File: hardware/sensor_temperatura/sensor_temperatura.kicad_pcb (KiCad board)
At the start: 2 copper layers, 18 x 59.1 mm, 7 parts, among them J1 Conn_01x04_Pin, J2 Conn_01x05_Pin, U1 ATtiny85-20P, U3 LM1117T-3.3

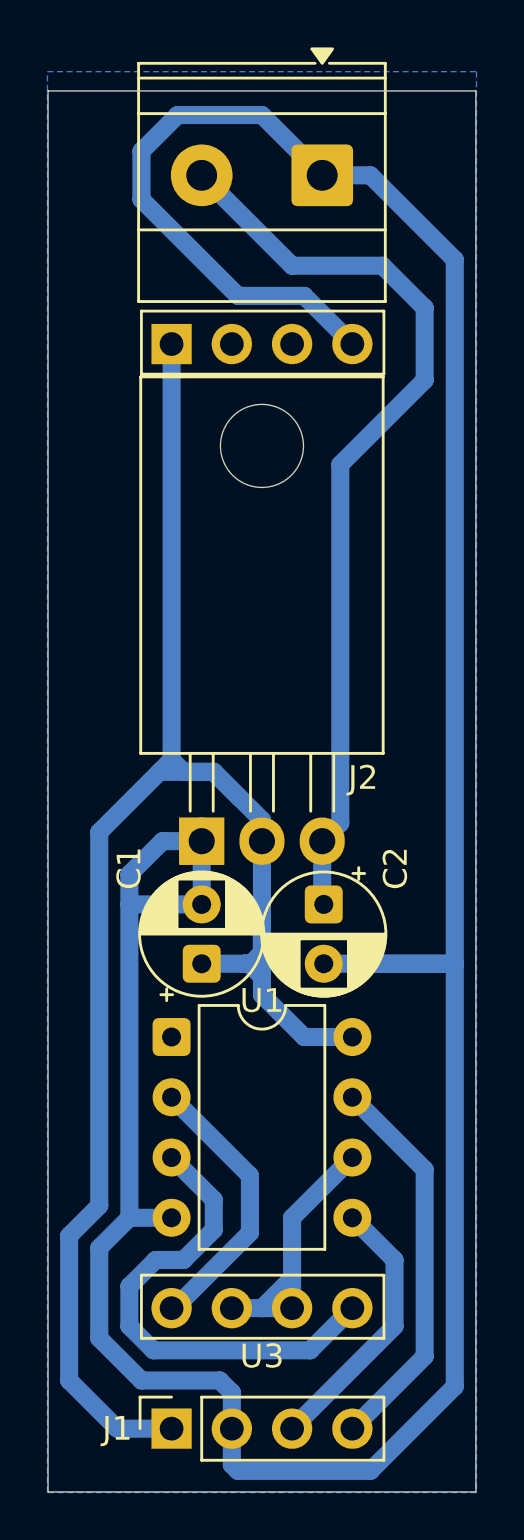
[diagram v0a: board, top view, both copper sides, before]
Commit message: Se actualiza modelo 3d para usar socalo para el micro.
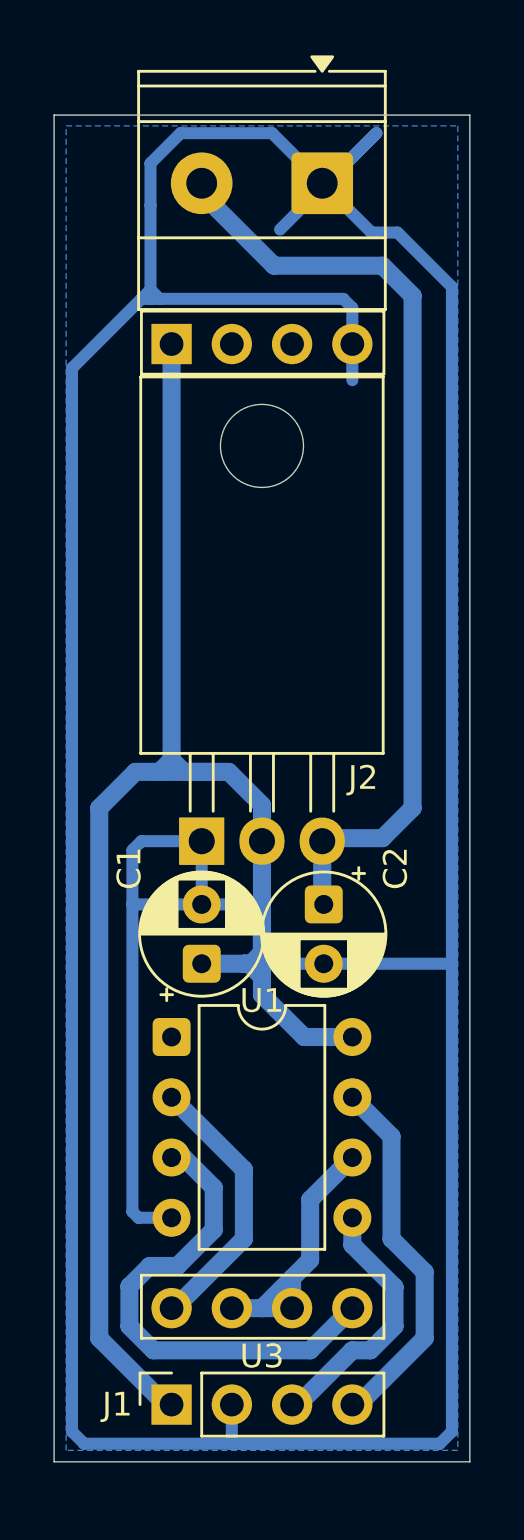
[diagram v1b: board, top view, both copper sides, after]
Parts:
- moved J1 1.02 mm to (158.8, 95.5)
- moved REF** 0.34 mm to (165.1, 44.0)
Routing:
- net GND: track 139.0 -> 194.6 mm
- net Net-(J1-VIN): track 77.3 -> 73.4 mm
- net +12V: track 38.8 -> 39.9 mm
- net Net-(J1-CL): track 16.5 -> 15.6 mm
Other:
- board size 18 x 59.1 mm -> 17.5 x 56.8 mm
